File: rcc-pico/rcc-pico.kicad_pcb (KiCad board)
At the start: 2 copper layers, 71.2 x 56 mm, 50 parts, among them J1 Conn_02x02_Odd_Even, J10 Conn_02x04_Odd_Even, J11 Conn_02x04_Odd_Even, J12 Conn_02x04_Odd_Even, J14 Conn_02x05_Odd_Even, J16 Conn_01x02_Pin, J3 PJ-006A, J5 Conn_3x4_female, J7 Conn_03x10, J8 Screw_Terminal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

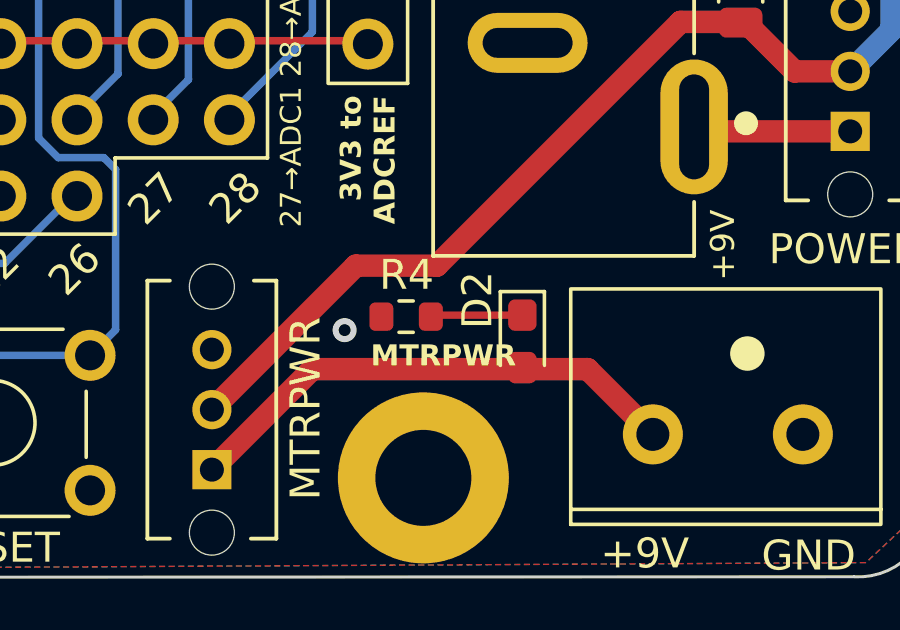
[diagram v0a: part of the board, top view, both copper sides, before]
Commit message: fixed D2 footprint
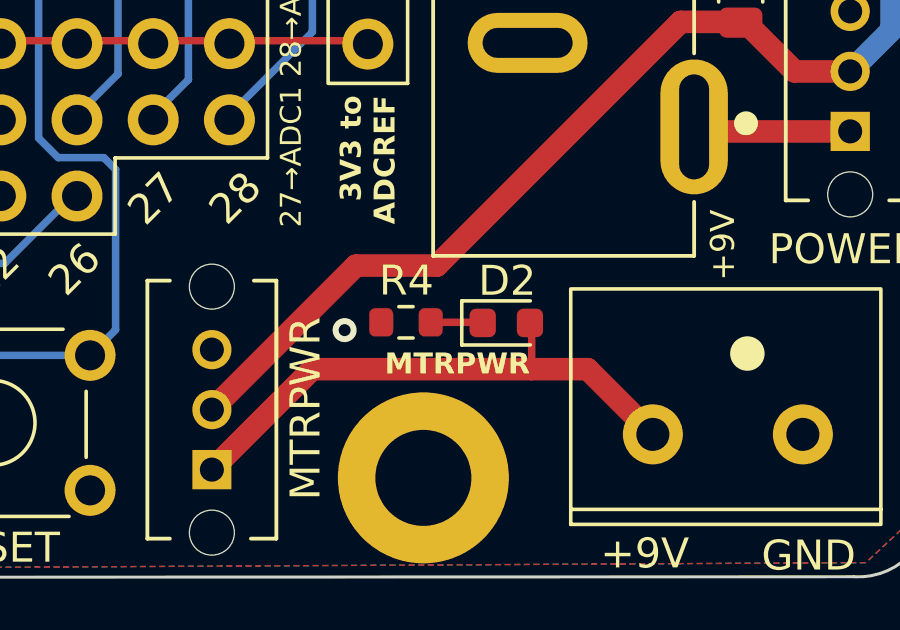
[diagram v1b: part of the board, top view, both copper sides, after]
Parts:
- D2: footprint LED_SMD:LED_0603_1608Metric_Pad1.05x0.95mm_HandSolder -> LED_SMD:LED_0603_1608Metric
- moved D2 0.82 mm to (133.3, 75.9), turned to 0 degrees
- moved R4 0.19 mm to (130.0, 75.9)
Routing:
- net /MTRPWR: track 17.0 -> 18.6 mm
- net Net-(D2-K): track 3.00 -> 1.74 mm
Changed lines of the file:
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@@
   )
   (footprint "Resistor_SMD:R_0603_1608Metric" (layer "F.Cu")
-    (at 129.975 75.7 180)
+    (at 129.97 75.89 180)
     (descr "Resistor SMD 0603 (1608 Metric), square (rectangular) end terminal, IPC_7351 nominal, (Body size source: IPC-SM-782 page 72, https://www.pcb-3d.com/wordpress/wp-content/uploads/ipc-sm-782a_amendment_1_and_2.pdf), generated with kicad-footprint-generator")
     (tags "resistor")
@@
     )
   )
-  (footprint "LED_SMD:LED_0603_1608Metric_Pad1.05x0.95mm_HandSolder" (layer "F.Cu")
-    (at 133.85 76.525 -90)
-    (descr "LED SMD 0603 (1608 Metric), square (rectangular) end terminal, IPC_7351 nominal, (Body size source: http://www.tortai-tech.com/upload/download/2011102023233369053.pdf), generated with kicad-footprint-generator")
-    (tags "LED handsolder")
-    (property "Sheetfile" "rcc-pico.kicad_sch")
-    (property "Sheetname" "")
-    (property "ki_description" "Light emitting diode")
-    (property "ki_keywords" "LED diode")
-    (attr smd)
-    (fp_text reference "D2" (at -1.375 1.5 90) (layer "F.SilkS")
-        (effects (font (size 1 1) (thickness 0.15)))
-    )
-    (fp_text value "LED" (at 0 1.43 90) (layer "F.Fab")
-        (effects (font (size 1 1) (thickness 0.15)))
-    )
-    (fp_text user "${REFERENCE}" (at 0 0 90) (layer "F.Fab")
-        (effects (font (size 0.4 0.4) (thickness 0.06)))
-    )
-    (fp_line (start -1.66 -0.735) (end -1.66 0.735)
-      (stroke (width 0.12) (type solid)) (layer "F.SilkS"))
-    (fp_line (start -1.66 0.735) (end 0.8 0.735)
-      (stroke (width 0.12) (type solid)) (layer "F.SilkS"))
-    (fp_line (start 0.8 -0.735) (end -1.66 -0.735)
-      (stroke (width 0.12) (type solid)) (layer "F.SilkS"))
-    (fp_line (start -1.65 -0.73) (end 1.65 -0.73)
-      (stroke (width 0.05) (type solid)) (layer "F.CrtYd"))
-    (fp_line (start -1.65 0.73) (end -1.65 -0.73)
-      (stroke (width 0.05) (type solid)) (layer "F.CrtYd"))
-    (fp_line (start 1.65 -0.73) (end 1.65 0.73)
-      (stroke (width 0.05) (type solid)) (layer "F.CrtYd"))
-    (fp_line (start 1.65 0.73) (end -1.65 0.73)
-      (stroke (width 0.05) (type solid)) (layer "F.CrtYd"))
-    (fp_line (start -0.8 -0.1) (end -0.8 0.4)
-      (stroke (width 0.1) (type solid)) (layer "F.Fab"))
-    (fp_line (start -0.8 0.4) (end 0.8 0.4)
-      (stroke (width 0.1) (type solid)) (layer "F.Fab"))
-    (fp_line (start -0.5 -0.4) (end -0.8 -0.1)
-      (stroke (width 0.1) (type solid)) (layer "F.Fab"))
-    (fp_line (start 0.8 -0.4) (end -0.5 -0.4)
-      (stroke (width 0.1) (type solid)) (layer "F.Fab"))
-    (fp_line (start 0.8 0.4) (end 0.8 -0.4)
-      (stroke (width 0.1) (type solid)) (layer "F.Fab"))
-    (pad "1" smd roundrect (at -0.875 0 270) (size 1.05 0.95) (layers "F.Cu" "F.Paste" "F.Mask") (roundrect_rratio 0.25)
-      (net 12 "Net-(D2-K)") (pinfunction "K") (pintype "passive"))
-    (pad "2" smd roundrect (at 0.875 0 270) (size 1.05 0.95) (layers "F.Cu" "F.Paste" "F.Mask") (roundrect_rratio 0.25)
-      (net 9 "/MTRPWR") (pinfunction "A") (pintype "passive"))
-    (model "${KICAD6_3DMODEL_DIR}/LED_SMD.3dshapes/LED_0603_1608Metric.wrl"
-      (offset (xyz 0 0 0))
-      (scale (xyz 1 1 1))
-      (rotate (xyz 0 0 0))
-    )
-  )
   (footprint "Resistor_SMD:R_0603_1608Metric" (layer "F.Cu")
     (at 124.45 49.4 180)
@@
       (net 2 "GND") (pintype "passive"))
     (model "${KICAD6_3DMODEL_DIR}/Capacitor_SMD.3dshapes/C_0805_2012Metric.wrl"
+      (offset (xyz 0 0 0))
+      (scale (xyz 1 1 1))
+      (rotate (xyz 0 0 0))
+    )
+  )
+  (footprint "LED_SMD:LED_0603_1608Metric" (layer "F.Cu")
+    (at 133.315 75.91)
+    (descr "LED SMD 0603 (1608 Metric), square (rectangular) end terminal, IPC_7351 nominal, (Body size source: http://www.tortai-tech.com/upload/download/2011102023233369053.pdf), generated with kicad-footprint-generator")
+    (tags "LED")
+    (property "Sheetfile" "rcc-pico.kicad_sch")
+    (property "Sheetname" "")
+    (property "ki_description" "Light emitting diode")
+    (property "ki_keywords" "LED diode")
+    (attr smd)
+    (fp_text reference "D2" (at 0.03 -1.4 180) (layer "F.SilkS")
+        (effects (font (size 1 1) (thickness 0.15)))
+    )
+    (fp_text value "LED" (at 0 1.43) (layer "F.Fab")
+        (effects (font (size 1 1) (thickness 0.15)))
+    )
+    (fp_text user "${REFERENCE}" (at 0 0) (layer "F.Fab")
+        (effects (font (size 0.4 0.4) (thickness 0.06)))
+    )
+    (fp_line (start -1.485 -0.735) (end -1.485 0.735)
+      (stroke (width 0.12) (type solid)) (layer "F.SilkS"))
+    (fp_line (start -1.485 0.735) (end 0.8 0.735)
+      (stroke (width 0.12) (type solid)) (layer "F.SilkS"))
+    (fp_line (start 0.8 -0.735) (end -1.485 -0.735)
+      (stroke (width 0.12) (type solid)) (layer "F.SilkS"))
+    (fp_line (start -1.48 -0.73) (end 1.48 -0.73)
+      (stroke (width 0.05) (type solid)) (layer "F.CrtYd"))
+    (fp_line (start -1.48 0.73) (end -1.48 -0.73)
+      (stroke (width 0.05) (type solid)) (layer "F.CrtYd"))
+    (fp_line (start 1.48 -0.73) (end 1.48 0.73)
+      (stroke (width 0.05) (type solid)) (layer "F.CrtYd"))
+    (fp_line (start 1.48 0.73) (end -1.48 0.73)
+      (stroke (width 0.05) (type solid)) (layer "F.CrtYd"))
+    (fp_line (start -0.8 -0.1) (end -0.8 0.4)
+      (stroke (width 0.1) (type solid)) (layer "F.Fab"))
+    (fp_line (start -0.8 0.4) (end 0.8 0.4)
+      (stroke (width 0.1) (type solid)) (layer "F.Fab"))
+    (fp_line (start -0.5 -0.4) (end -0.8 -0.1)
+      (stroke (width 0.1) (type solid)) (layer "F.Fab"))
+    (fp_line (start 0.8 -0.4) (end -0.5 -0.4)
+      (stroke (width 0.1) (type solid)) (layer "F.Fab"))
+    (fp_line (start 0.8 0.4) (end 0.8 -0.4)
+      (stroke (width 0.1) (type solid)) (layer "F.Fab"))
+    (pad "1" smd roundrect (at -0.7875 0) (size 0.875 0.95) (layers "F.Cu" "F.Paste" "F.Mask") (roundrect_rratio 0.25)
+      (net 12 "Net-(D2-K)") (pinfunction "K") (pintype "passive"))
+    (pad "2" smd roundrect (at 0.7875 0) (size 0.875 0.95) (layers "F.Cu" "F.Paste" "F.Mask") (roundrect_rratio 0.25)
+      (net 9 "/MTRPWR") (pinfunction "A") (pintype "passive"))
+    (model "${KICAD6_3DMODEL_DIR}/LED_SMD.3dshapes/LED_0603_1608Metric.wrl"
       (offset (xyz 0 0 0))
       (scale (xyz 1 1 1))
@@
     (effects (font (size 0.9 0.9) (thickness 0.14)) (justify left bottom))
   )
-  (gr_text "MTRPWR" (at 128.79 77.41) (layer "F.SilkS")
+  (gr_text "MTRPWR" (at 129.26 77.68) (layer "F.SilkS")
     (effects (font (size 0.7 0.7) (thickness 0.12) bold) (justify left bottom))
   )
@@
   (segment (start 134.175 36.7875) (end 135.4925 36.7875) (width 0.25) (layer "F.Cu") (net 8))
   (segment (start 123.5 80.8) (end 126.85 77.45) (width 0.75) (layer "F.Cu") (net 9))
+  (segment (start 126.85 77.45) (end 134.16 77.45) (width 0.75) (layer "F.Cu") (net 9))
+  (segment (start 134.16 77.45) (end 136.025 77.45) (width 0.75) (layer "F.Cu") (net 9))
   (segment (start 136.025 77.45) (end 138.2 79.625) (width 0.75) (layer "F.Cu") (net 9))
-  (segment (start 126.85 77.45) (end 136.025 77.45) (width 0.75) (layer "F.Cu") (net 9))
+  (segment (start 134.16 75.9675) (end 134.16 77.45) (width 0.25) (layer "F.Cu") (net 9))
+  (segment (start 134.1025 75.91) (end 134.16 75.9675) (width 0.25) (layer "F.Cu") (net 9))
   (segment (start 111.6 56.625) (end 111.6 55.625) (width 0.25) (layer "F.Cu") (net 10))
   (segment (start 111.5875 55.6125) (end 111.5875 53.05) (width 0.25) (layer "F.Cu") (net 10))
@@
   (segment (start 102.555 59.295) (end 102.555 60.685) (width 0.25) (layer "B.Cu") (net 11))
   (segment (start 105.2995 56.6) (end 105.25 56.6) (width 0.25) (layer "B.Cu") (net 11))
-  (segment (start 130.85 75.65) (end 133.85 75.65) (width 0.25) (layer "F.Cu") (net 12))
+  (segment (start 132.5075 75.89) (end 132.5275 75.91) (width 0.25) (layer "F.Cu") (net 12))
+  (segment (start 130.795 75.89) (end 132.5075 75.89) (width 0.25) (layer "F.Cu") (net 12))
   (segment (start 117.725 61.125) (end 118.97 59.88) (width 0.25) (layer "B.Cu") (net 13))
   (segment (start 119.9 70.4) (end 118.375 70.4) (width 0.25) (layer "B.Cu") (net 13))

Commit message: final touches, fixed footprints
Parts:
- R10, R5, R6, R7, R8, R9: footprint Resistor_SMD:R_0603_1608Metric_Pad0.98x0.95mm_HandSolder -> Resistor_SMD:R_0603_1608Metric
- moved R8 2.99 mm to (102.0, 53.8), turned to 90 degrees
- moved R10 2.97 mm to (96.2, 53.8), turned to 90 degrees
- moved R6 2.87 mm to (107.9, 53.6), turned to 90 degrees
- moved D1 1.04 mm to (133.5, 38.4), turned to 0 degrees
- moved R7 0.94 mm to (102.0, 57.4)
- moved R9 0.87 mm to (96.2, 57.3)
- moved R5 0.82 mm to (107.8, 57.3)
- moved R3 0.10 mm to (130.0, 38.4)
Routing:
- net /SCL: track 33.8 -> 26.3 mm
- net +3.3V: track 167.3 -> 163.2 mm
- net /5V_PWM_1: track 19.2 -> 23.0 mm, vias 1 -> 2
- net /3V3_PWM_2: track 21.2 -> 24.6 mm, vias 1 -> 3
- net /3V3_PWM_3: track 23.2 -> 25.9 mm, vias 1 -> 3
- net /3V3_PWM_1: track 27.5 -> 30.0 mm
- net /5V_PWM_3: track 13.1 -> 11.4 mm
- net Net-(D1-K): track 3.21 -> 1.84 mm
- net GND: vias 53 -> 54

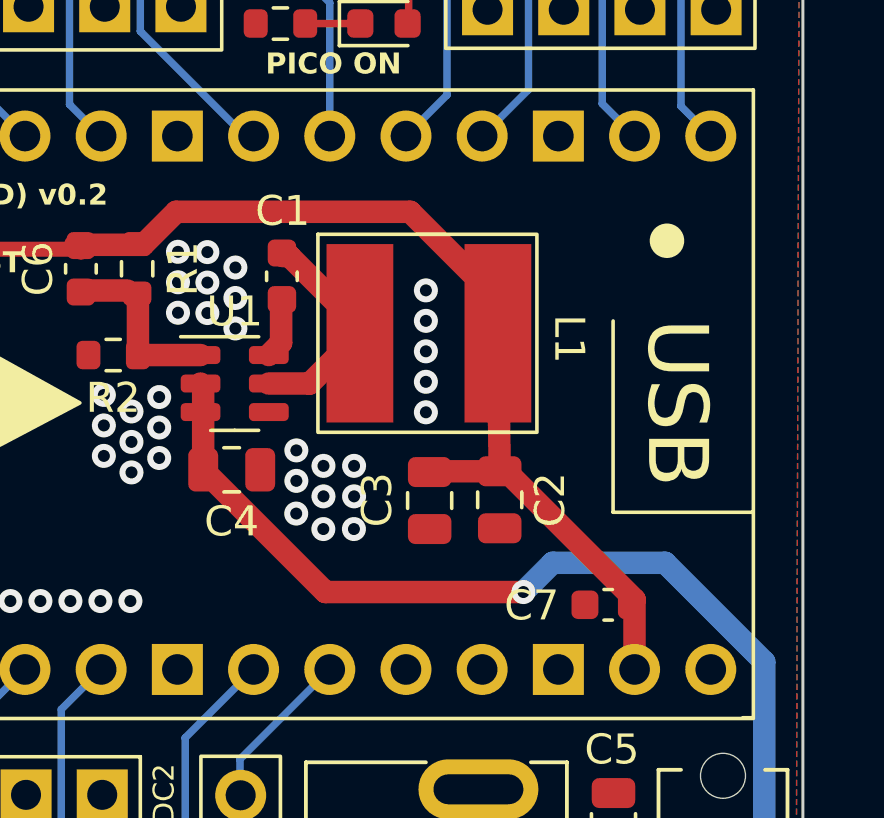
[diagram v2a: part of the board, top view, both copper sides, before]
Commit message: changed 0.1uH footprint, added v0.2 BOM
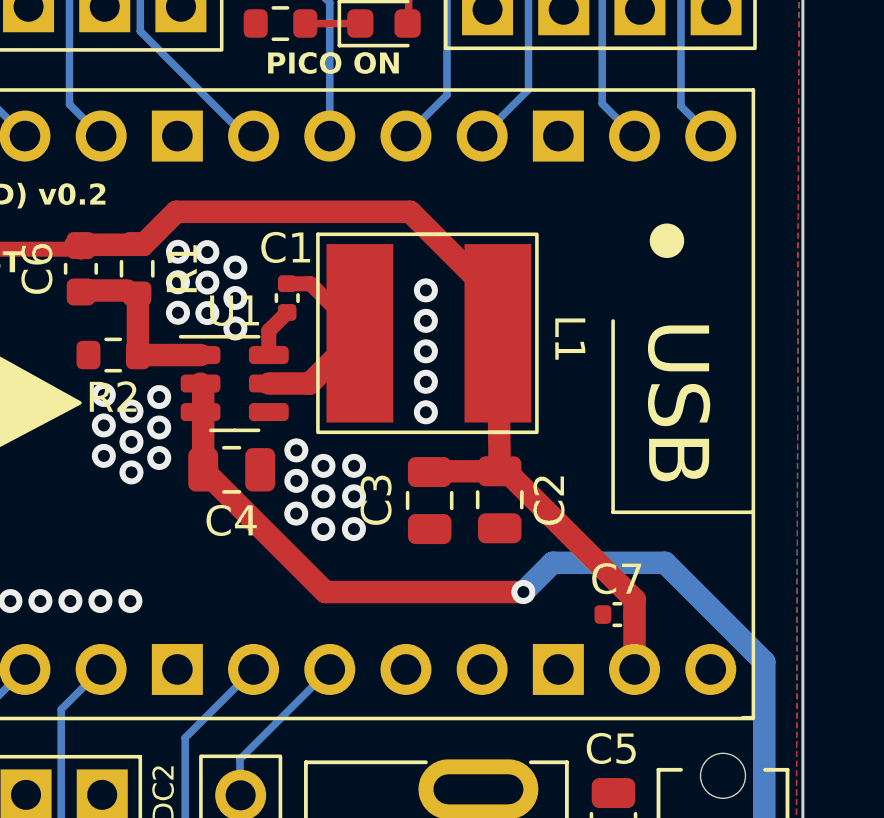
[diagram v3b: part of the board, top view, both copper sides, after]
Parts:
- C1, C7: footprint Capacitor_SMD:C_0603_1608Metric -> Capacitor_SMD:C_0402_1005Metric
- moved C1 0.75 mm to (130.2, 47.5)
- moved C7 0.45 mm to (141.3, 58.0)

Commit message: ordering v0.2
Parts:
- added TP1: TestPoint, Connector_PinHeader_2.54mm:PinHeader_1x01_P2.54mm_Vertical, F.Cu at (81.1, 71.0)
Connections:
- H1 pad 1: GND -> unconnected-(H1-Pad1)
- H2 pad 1: GND -> unconnected-(H2-Pad1)
- H3 pad 1: GND -> unconnected-(H3-Pad1)
- H4 pad 1: GND -> unconnected-(H4-Pad1)
- J4 pad 25: /GPIO27 -> /GPIO26
- J4 pad 26: /GPIO28 -> /GPIO27
- J4 pad 3: /GPIO26 -> /GPIO28
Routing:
- net /GPIO28: track 11.2 -> 18.2 mm
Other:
- outline, holes or cut-outs redrawn
- board text added: "*28"
- board text added: "Connect Pins To Use *Extras* 14&15→I2C1 Bus 16,17,18→5V~PWM 22→Button 28→Potentiometer"
- board text removed: "*26"
- board text removed: "Connect Pins To Use *Extras* 14&15→I2C1 Bus 16,17,18→5V~PWM 22→Button 26→Potentiometer"

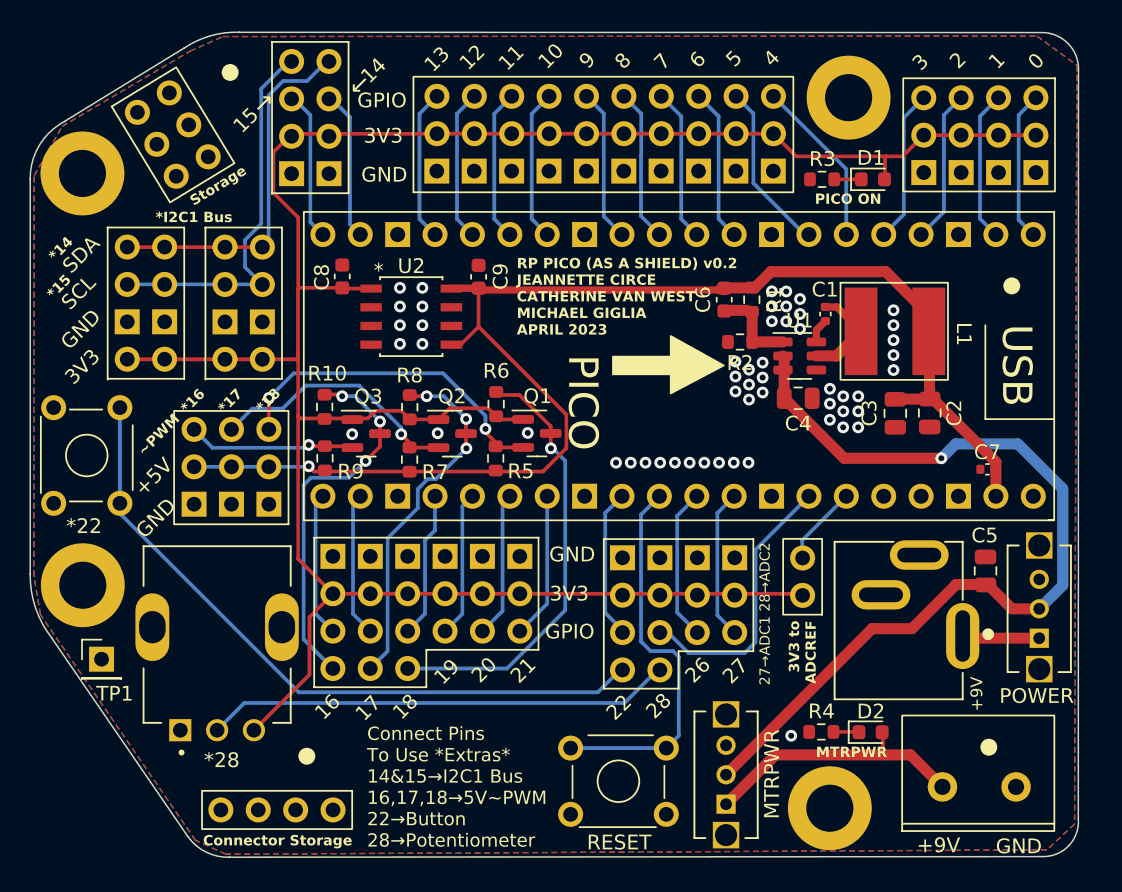
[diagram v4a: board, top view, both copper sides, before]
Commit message: v0.3 modifications, added input protection diode
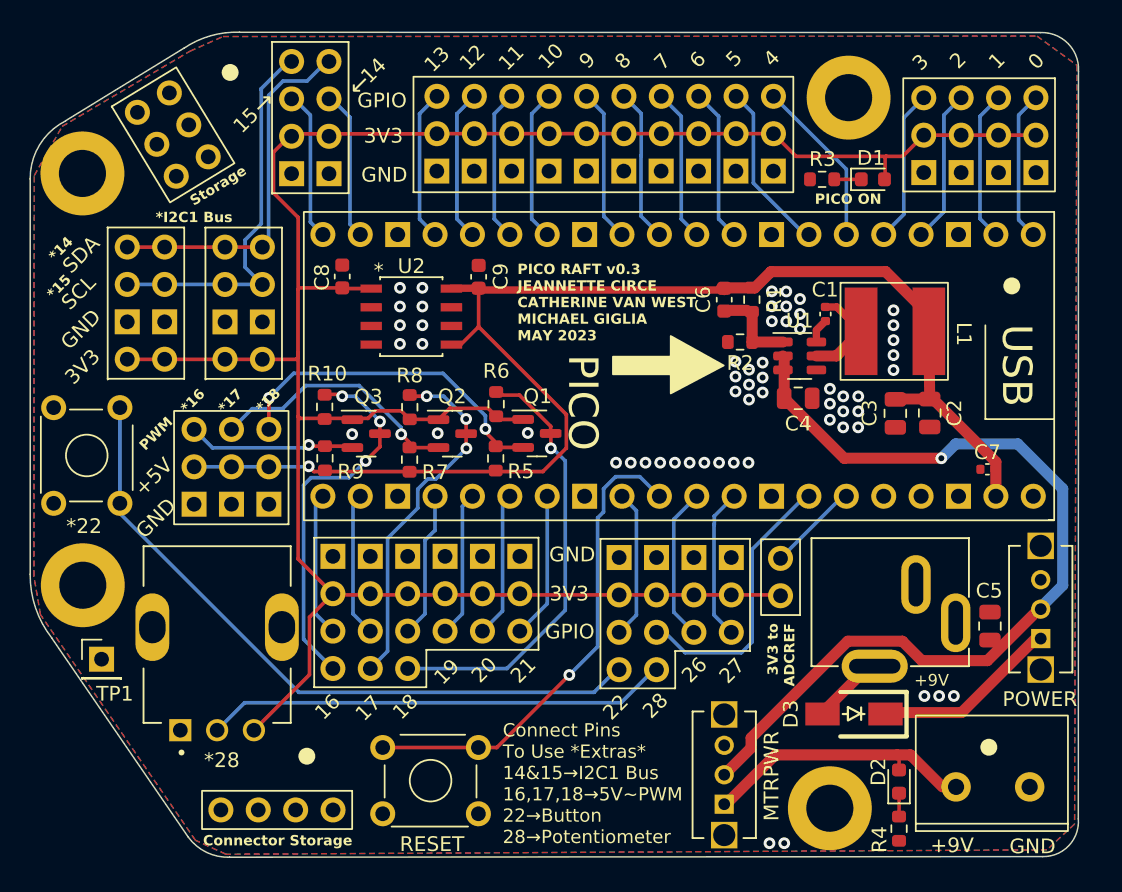
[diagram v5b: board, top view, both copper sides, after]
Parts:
- added D3: D_Schottky, custom-components:DIOM5227X270N, F.Cu at (132.2, 74.7)
- moved SW1 12.8 mm to (100.2, 77.0)
- moved R4 8.43 mm to (135.2, 82.5), turned to -90 degrees
- moved J3 6.32 mm to (133.6, 71.4), turned to 180 degrees
- moved D2 3.87 mm to (135.2, 79.3), turned to 90 degrees
- moved C5 3.76 mm to (141.4, 68.7)
- moved J16 1.50 mm to (127.2, 64.1)
- moved J8 0.93 mm to (141.6, 85.3)
- moved J4 0.23 mm to (120.0, 75.5)
- moved SW-on/off2 0.12 mm to (123.4, 78.8)
- moved SW-on/off1 0.10 mm to (144.9, 67.5)
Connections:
- J3 pad 1: Net-(SW-on/off1-A) -> Net-(D3-A)
- SW-on/off1 pad 1: Net-(SW-on/off1-A) -> Net-(D3-K)
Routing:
- net Net-(D3-K): track 0.00 -> 12.6 mm
- net /run: track 26.4 -> 33.0 mm, vias 0 -> 1
- net Net-(SW-on/off1-A): track 5.05 -> 0.00 mm
- net Net-(D3-A): track 0.00 -> 4.86 mm
- net +3.3V: track 162.8 -> 162.1 mm
- net GND: vias 54 -> 58
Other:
- board text added: "PICO RAFT v0.3 JEANNETTE CIRCE CATHERINE VAN WEST MICHAEL GIGLIA MAY 2023"
- board text added: "PWM"
- board text removed: "27→ADC1 28→ADC2"
- board text removed: "RP PICO (AS A SHIELD) v0.2 JEANNETTE CIRCE CATHERINE VAN WEST MICHAEL GIGLIA APRIL 2023"
- board text removed: "~PWM"
